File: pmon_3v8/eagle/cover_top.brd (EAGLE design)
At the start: 66 x 66 mm, 2 parts

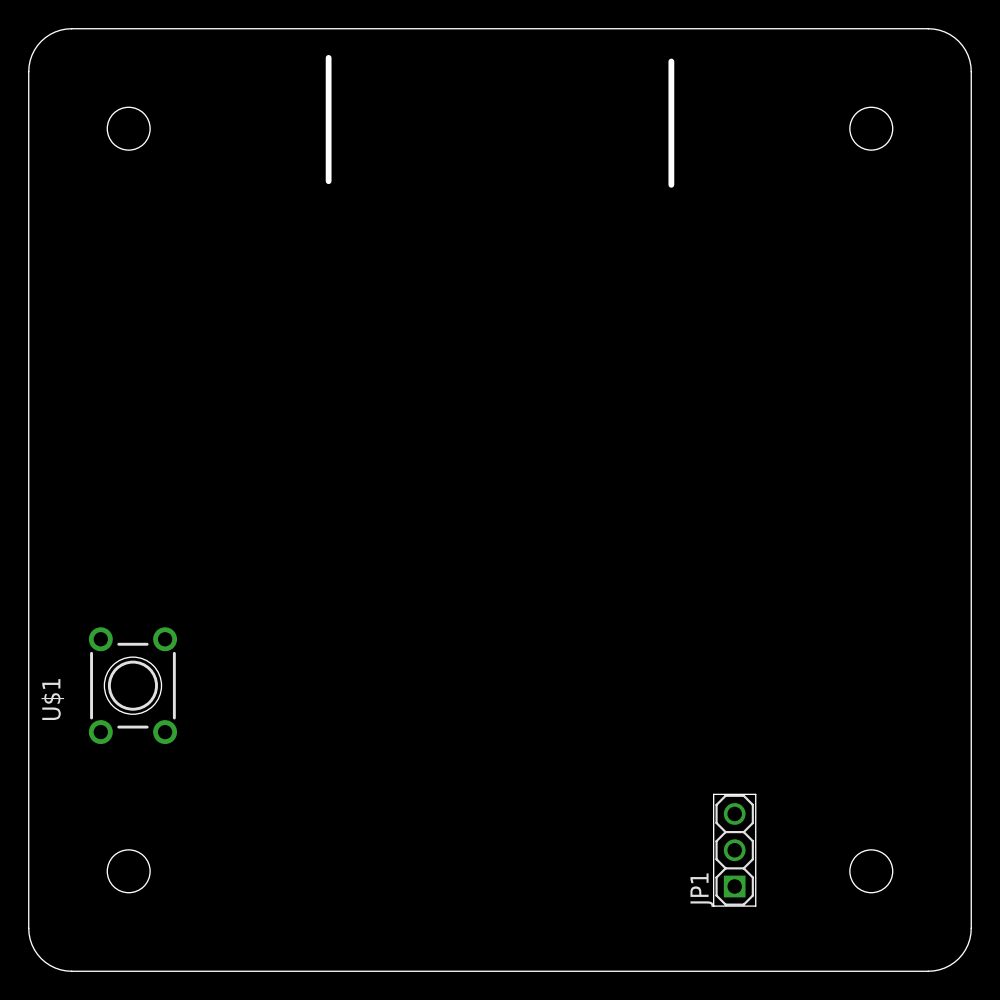
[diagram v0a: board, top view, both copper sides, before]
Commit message: Renamed power play oled to power play 3.8V (to be consistent with the 5V name of the other variant).
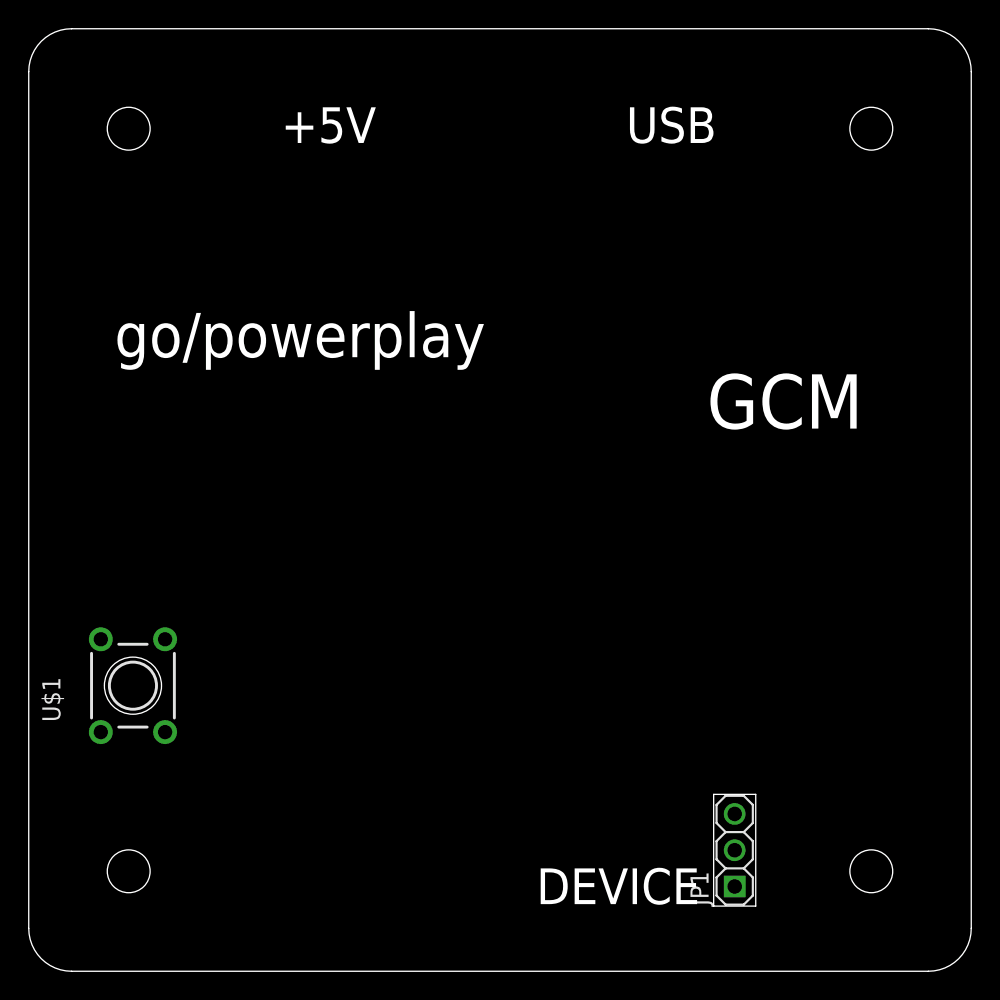
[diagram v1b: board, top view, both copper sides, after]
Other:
- outline, holes or cut-outs redrawn
- board text added: "+5V"
- board text added: "DEVICE"
- board text added: "GCM"
- board text added: "USB"
- board text added: "go/powerplay"
